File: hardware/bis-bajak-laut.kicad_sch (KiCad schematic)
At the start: 1 part, among them U1 RP2040

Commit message: feat: copying schematic part 1
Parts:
- added C1, C2, C3, C4, C6, C8: 100nF, Capacitor_SMD:C_0805_2012Metric_Pad1.18x1.45mm_HandSolder, symbol Device:C
- added C5, C7, C9: 2.2uF, Capacitor_SMD:C_0805_2012Metric_Pad1.18x1.45mm_HandSolder, symbol Device:C
- added D2, D3, D4, D5, D6: BAS40-05T, symbol Device:D_Schottky_Dual_CommonCathode_AAK
- added J1: TFT, symbol Connector_Generic:Conn_01x09
- added Q1, Q2, Q3, Q4, Q5, Q6, Q7, Q8: Q_PMOS_GSD, symbol Device:Q_PMOS_GSD
- added Q9: Q_NMOS_GSD, symbol Device:Q_NMOS_GSD
- added R1: 10K, Resistor_SMD:R_0805_2012Metric_Pad1.20x1.40mm_HandSolder, symbol Device:R_US
- added R10, R11, R12, R13, R14, R2, R25, R26, R27, R28, R29, R3, R30, R31, R32, R33, R34, R35, R36, R4, R5, R6, R7, R8, R9: 510, Resistor_SMD:R_0805_2012Metric_Pad1.20x1.40mm_HandSolder, symbol Device:R_US
- added R15, R16, R17, R18, R19, R20, R21, R22, R23, R24, R37, R38: 10k, Resistor_SMD:R_0805_2012Metric_Pad1.20x1.40mm_HandSolder, symbol Device:R_US
- added R39: 100K, Resistor_SMD:R_0805_2012Metric_Pad1.20x1.40mm_HandSolder, symbol Device:R_US
- added R40: 200, Resistor_SMD:R_0805_2012Metric_Pad1.20x1.40mm_HandSolder, symbol Device:R_US
- added R41: 33, Resistor_SMD:R_0805_2012Metric_Pad1.20x1.40mm_HandSolder, symbol Device:R_US
- added U2, U6: 74HC595, Package_SO:SOIC-16_3.9x9.9mm_P1.27mm, symbol 74xx:74HC595
- added U3, U7, U8: LMV324, Package_SO:SOIC-14_3.9x8.7mm_P1.27mm, symbol Amplifier_Operational:LMV324
- added U4: CD74HC4067M, Package_SO:SOIC-24W_7.5x15.4mm_P1.27mm, symbol 74xx:CD74HC4067M
- added U5: 74HC245, Package_DIP:DIP-20_W8.89mm_SMDSocket_LongPads, symbol 74xx:74HC245
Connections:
- new net: R26.1, U4.8 (I1)
- new net: Q1.3 (D), R16.1
- new net: Q4.3 (D), R17.1
- new net: R3.1, U5.17 (B1)
- new net: U2.1 (QB), U5.6 (A4)
- new net: U2.15 (QA), U5.2 (A0)
- new net: U2.2 (QC), U5.5 (A3)
- new net: U2.3 (QD), U5.4 (A2)
- new net: U2.4 (QE), U5.3 (A1)
- new net: U2.7 (QH), U5.9 (A7)
- new net: U2.9 (QH'), U6.14 (SER)
- new net: Q3.3 (D), R15.1
- new net: D4.2 (A), R12.2, U7.5 (+)
- new net: D4.1 (A), R11.2, U7.3 (+)
- new net: D5.2 (A), R14.2, U7.12 (+)
- new net: R28.1, U4.6 (I3)
- new net: D3.1 (A), R8.2, U3.10 (+)
- new net: R2.1, U5.18 (B0)
- new net: U4.1 (COM), U8.3 (+)
- new net: R32.1, U4.2 (I7)
- new net: R36.1, U4.20 (I11)
- new net: R35.1, U4.21 (I10)
- new net: R34.1, U4.22 (I9)
- new net: R33.1, U4.23 (I8)
- new net: R31.1, U4.3 (I6)
- new net: R30.1, U4.4 (I5)
- new net: R29.1, U4.5 (I4)
- new net: R27.1, U4.7 (I2)
- new net: R25.1, U4.9 (I0)
- new net: D3.2 (A), R9.2, U3.12 (+)
- new net: D5.1 (A), R13.2, U7.10 (+)
- new net: D2.1 (A), R7.2, U3.3 (+)
- new net: D2.2 (A), R10.2, U3.5 (+)
- new net: R5.1, U5.15 (B3)
- new net: Q7.3 (D), R23.1
- new net: Q8.3 (D), R21.1
- new net: Q9.1 (G), R40.1
- new net: Q5.3 (D), R20.1
- new net: Q9.3 (D), R41.2
- new net: R6.1, U5.14 (B4)
- new net: Q6.3 (D), R22.1
- new net: D6.1 (A), R39.1, U8.5 (+)
- new net: R4.1, U5.16 (B2)
- new net: Q2.3 (D), R18.1
- new net: R37.2, U8.1, U8.2 (-)
- new net +3V3: C1.1, C2.1, C3.1, J1.4 (Pin_4), R1.1, U2.10 (~{SRCLR}), U2.16 (VCC), U5.20 (VCC), U6.10 (~{SRCLR}), U6.16 (VCC)
- new net AMUX_EN: R2.2, R24.2, U4.15 (~{E})
- new net AMUX_OUT: R37.1, R38.1
- new net AMUX_S0: R6.2, U4.10 (S0)
- new net AMUX_S1: R5.2, U4.11 (S1)
- new net AMUX_S2: R4.2, U4.14 (S2)
- new net AMUX_S3: R3.2, U4.13 (S3)
- new net BPIO0: R14.1, R23.2
- new net BPIO1: R13.1, R22.2
- new net BPIO2: R12.1, R21.2
- new net BPIO3: R11.1, R20.2
- new net BPIO4: R18.2, R9.1
- new net BPIO5: R17.2, R8.1
- new net BPIO6: R10.1, R16.2
- new net BPIO7: R15.2, R7.1
- new net CURRENT_EN: U6.1 (QB)
- new net CURRENT_EN_OVERRIDE: U6.5 (QF)
- new net CURRENT_RESET: U6.3 (QD)
- new net DAC_RESET: U6.4 (QE)
- new net DISPLAY_BACKLIGHT: R40.2, U2.5 (QF)
- new net DISPLAY_CS: J1.6 (Pin_6)
- new net DISPLAY_DP: J1.5 (Pin_5)
- new net DISPLAY_LED_K: J1.2 (Pin_2), R41.1
- new net DISPLAY_RESET: J1.9 (Pin_9), U2.6 (QG)
- new net GND: C1.2, C2.2, C3.2, C4.2, C5.2, C6.2, C7.2, C8.2, C9.2, J1.1 (Pin_1), Q9.2 (S), R38.2, U2.8 (GND), U3.11 (V-), U4.12 (GND), U4.16 (I15), U4.17 (I14), U4.18 (I13), U4.19 (I12), U5.10 (GND), U5.8 (A6), U6.8 (GND), U7.11 (V-), U8.11 (V-)
- new net LEDS_CD0: U5.13 (B5)
- new net MUX_BPIO0: U7.13 (-), U7.14
- new net MUX_BPIO1: U7.8, U7.9 (-)
- new net MUX_BPIO2: U7.6 (-), U7.7
- new net MUX_BPIO3: U7.1, U7.2 (-)
- new net MUX_BPIO4: U3.13 (-), U3.14
- new net MUX_BPIO5: U3.8, U3.9 (-)
- new net MUX_BPIO6: U3.6 (-), U3.7
- new net MUX_BPIO7: U3.1, U3.2 (-)
- new net MUX_VREF_OUT: U8.6 (-), U8.7
- new net PULLUP_EN: Q1.1 (G), Q2.1 (G), Q3.1 (G), Q4.1 (G), Q5.1 (G), Q6.1 (G), Q7.1 (G), Q8.1 (G), R19.1, U5.11 (B7)
- new net RGB_CD0: U5.7 (A5)
- new net SHIFT_EN: R1.2, U2.13 (~{OE}), U5.19 (CE), U6.13 (~{OE})
- new net SHIFT_LATCH: U2.12 (RCLK), U6.12 (RCLK)
- new net SPI_CD0: J1.8 (Pin_8), U2.14 (SER)
- new net SPI_CLK: J1.7 (Pin_7), U2.11 (SRCLK), U6.11 (SRCLK)
- new net VBUS: C4.1, C5.1, C6.1, C7.1, C8.1, C9.1, D2.3 (K), D3.3 (K), D4.3 (K), D5.3 (K), D6.3 (K), J1.3 (Pin_3), R19.2, R24.1, U3.4 (V+), U4.24 (VCC), U5.1 (A->B), U7.4 (V+), U8.4 (V+)
- new net VREF_OUT: Q1.2 (S), Q2.2 (S), Q3.2 (S), Q4.2 (S), Q5.2 (S), Q6.2 (S), Q7.2 (S), Q8.2 (S), R39.2
- no-connect marks 0 -> 7
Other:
- company: (none) -> Crumbs Module
- title: (none) -> Bis Bajak Laut - Bus Pirate Copy From Scratch
- moved on the sheet: U1

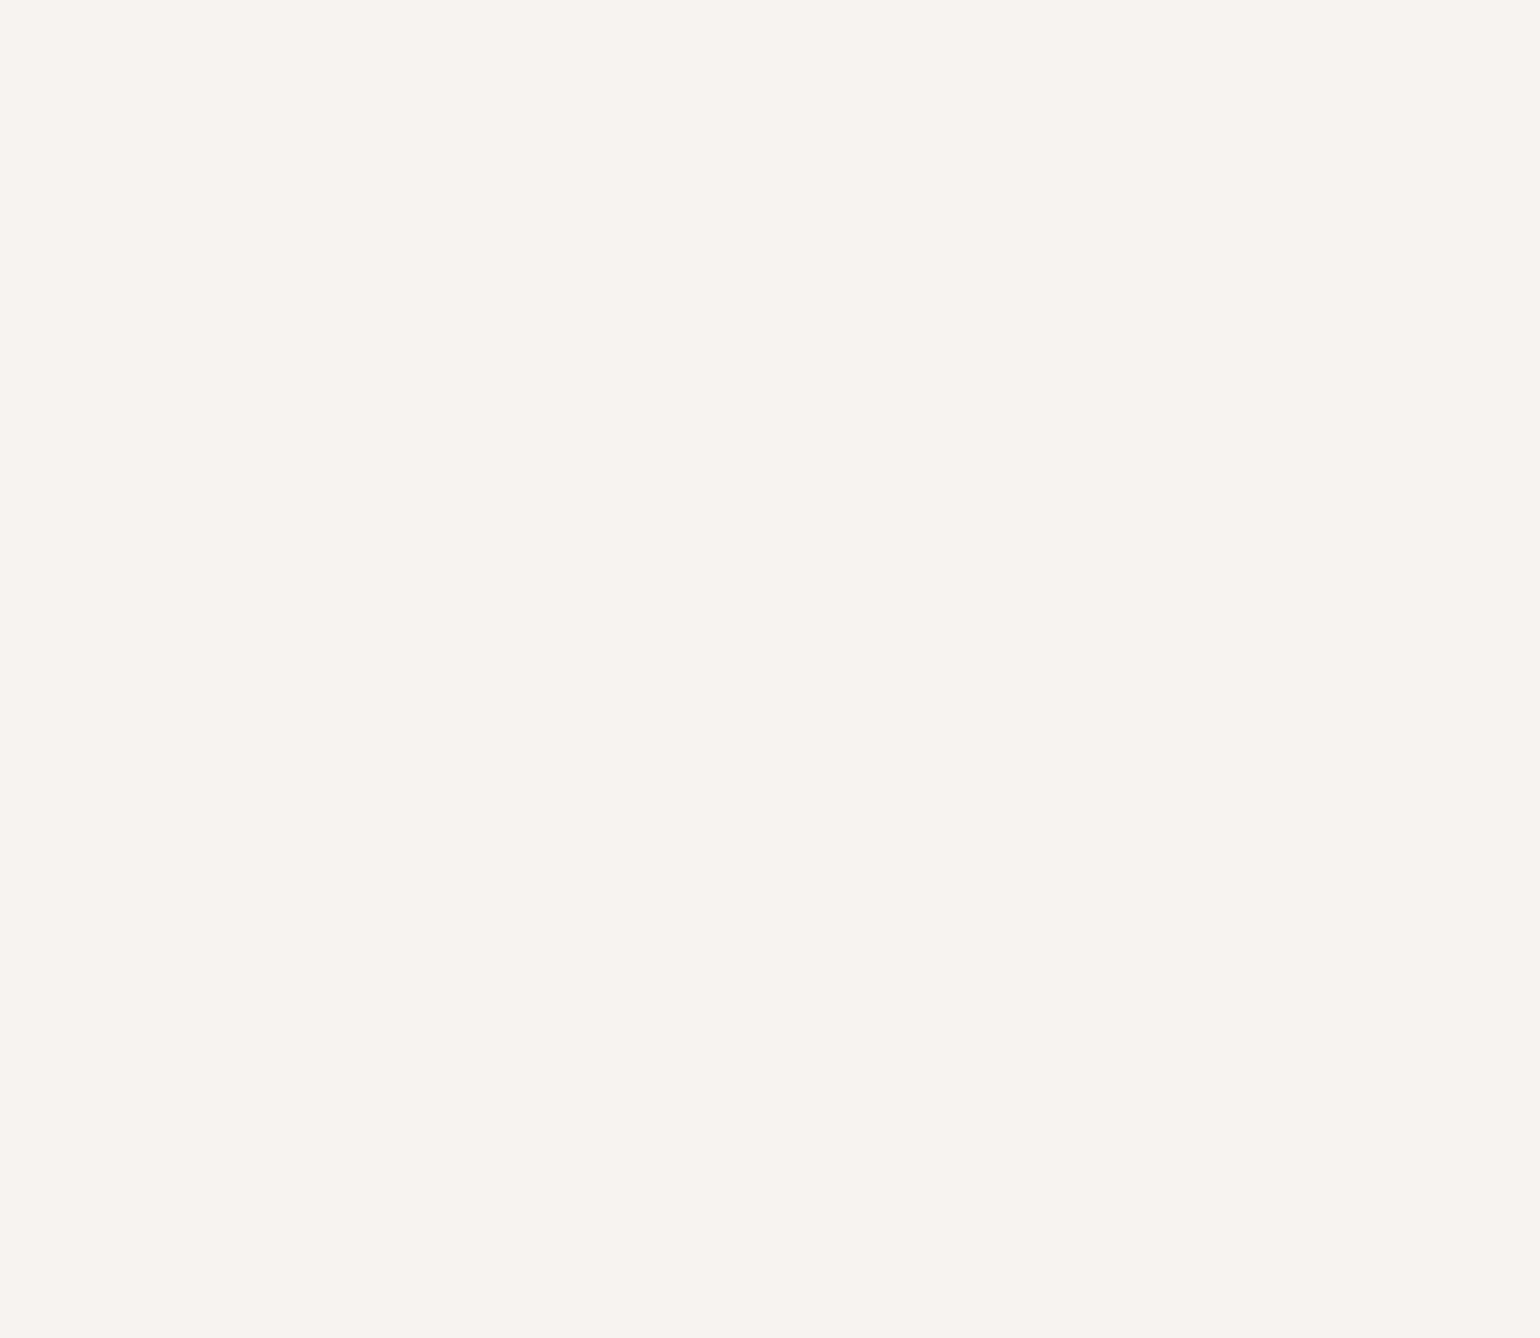
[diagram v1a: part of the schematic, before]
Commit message: feat: copying schematic part 2
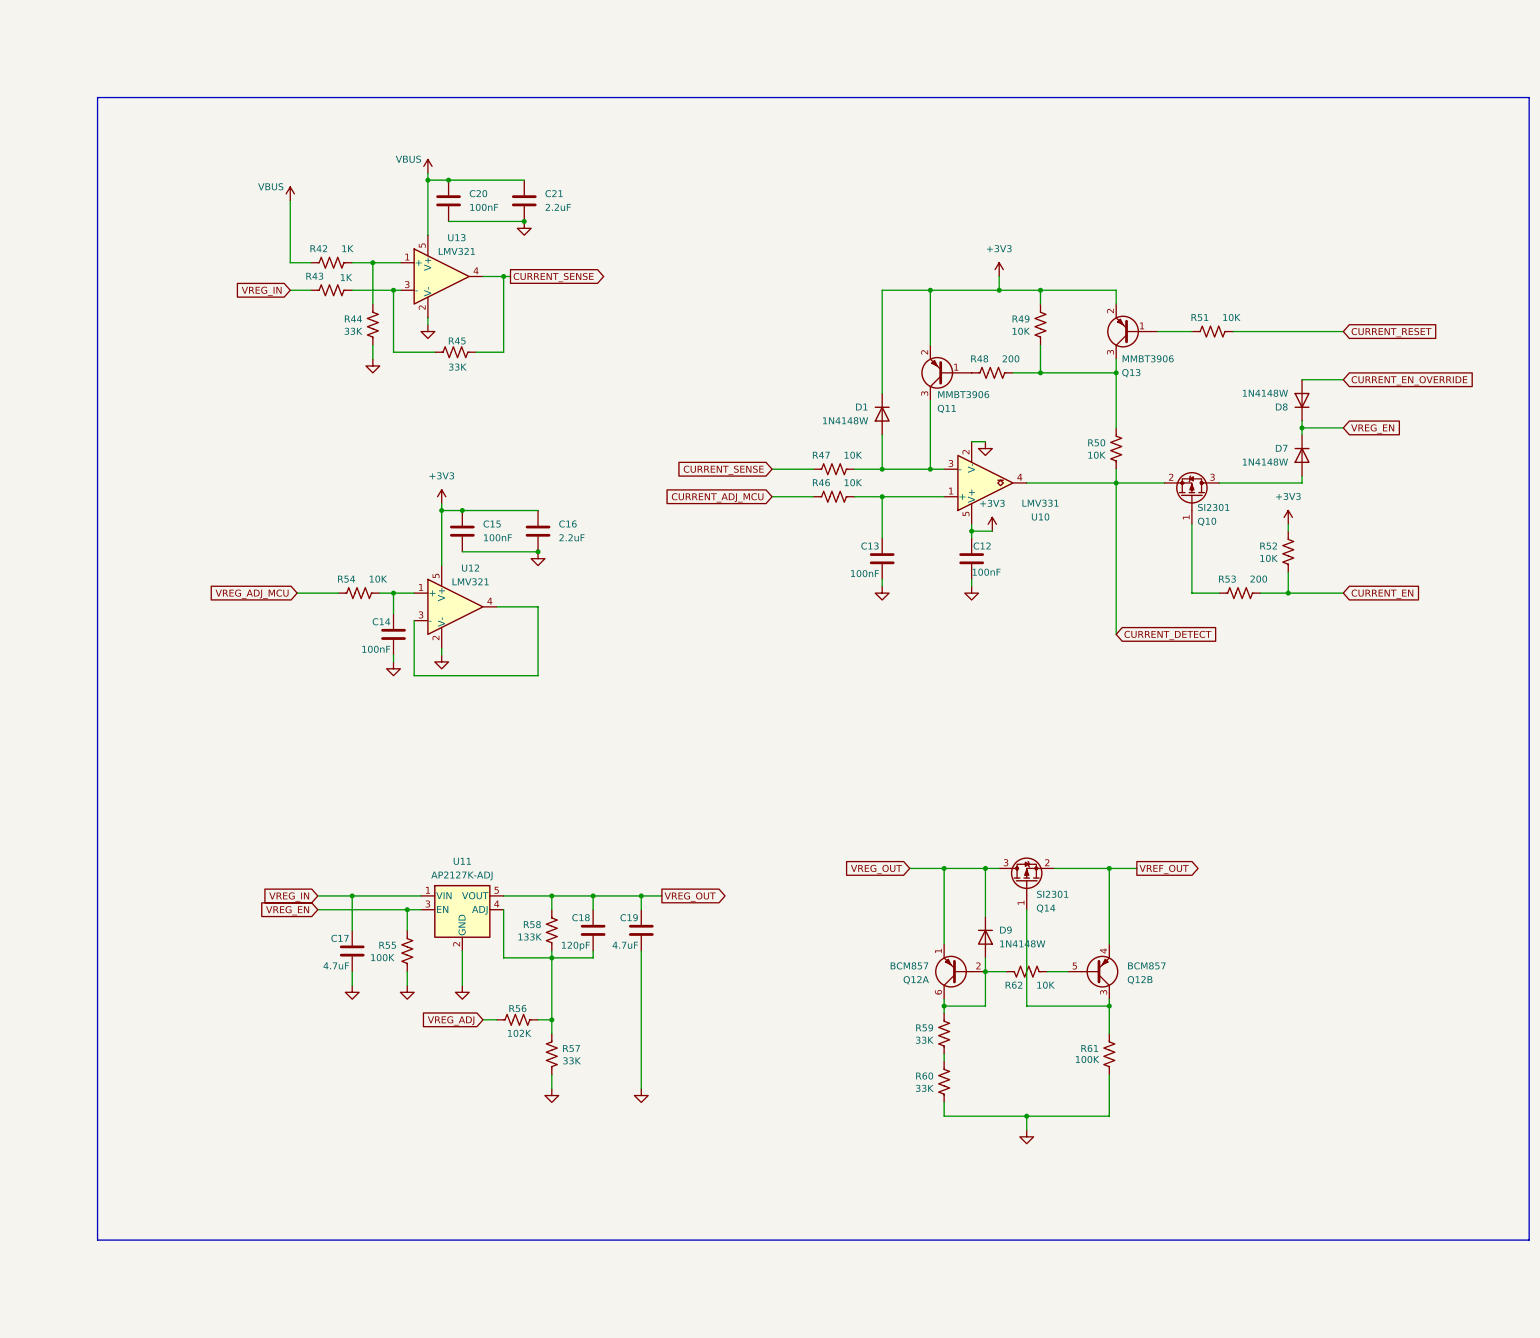
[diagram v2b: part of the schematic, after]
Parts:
- added C12, C13, C14, C15, C20: 100nF, Capacitor_SMD:C_0805_2012Metric_Pad1.18x1.45mm_HandSolder, symbol Device:C
- added C16, C21: 2.2uF, Capacitor_SMD:C_0805_2012Metric_Pad1.18x1.45mm_HandSolder, symbol Device:C
- added C17, C19: 4.7uF, Capacitor_SMD:C_0805_2012Metric_Pad1.18x1.45mm_HandSolder, symbol Device:C
- added C18: 120pF, Capacitor_SMD:C_0805_2012Metric_Pad1.18x1.45mm_HandSolder, symbol Device:C
- added D1, D7, D8, D9: 1N4148W, Diode_SMD:D_SOD-123, symbol Diode:1N4148W
- added Q10, Q14: SI2301, symbol Device:Q_PMOS_GSD
- added Q11, Q13: MMBT3906, Package_TO_SOT_SMD:SOT-23, symbol Transistor_BJT:MMBT3906
- added Q12: BCM857, Package_TO_SOT_SMD:SOT-363_SC-70-6_Handsoldering, symbol Device:Q_Dual_PNP_PNP_E1B1C2E2B2C1
- added R42, R43: 1K, Resistor_SMD:R_0805_2012Metric_Pad1.20x1.40mm_HandSolder, symbol Device:R_US
- added R44, R45, R57, R59, R60: 33K, Resistor_SMD:R_0805_2012Metric_Pad1.20x1.40mm_HandSolder, symbol Device:R_US
- added R46, R47, R49, R50, R51, R52, R54, R62: 10K, Resistor_SMD:R_0805_2012Metric_Pad1.20x1.40mm_HandSolder, symbol Device:R_US
- added R48, R53: 200, Resistor_SMD:R_0805_2012Metric_Pad1.20x1.40mm_HandSolder, symbol Device:R_US
- added R55, R61: 100K, Resistor_SMD:R_0805_2012Metric_Pad1.20x1.40mm_HandSolder, symbol Device:R_US
- added R56: 102K, Resistor_SMD:R_0805_2012Metric_Pad1.20x1.40mm_HandSolder, symbol Device:R_US
- added R58: 133K, Resistor_SMD:R_0805_2012Metric_Pad1.20x1.40mm_HandSolder, symbol Device:R_US
- added U10: LMV331, Package_TO_SOT_SMD:SOT-23-5_HandSoldering, symbol Comparator:LMV331
- added U11: AP2127K-ADJ, Package_TO_SOT_SMD:SOT-23-5, symbol Regulator_Linear:AP2127K-ADJ
- added U12, U13: LMV321, symbol Amplifier_Operational:LMV321
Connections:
- net +3V3: now also C12.1, C15.1, C16.1, D1.1 (K), Q11.2 (E), Q13.2 (E), R49.1, R52.1, U10.5 (V+), U12.5 (V+)
- net CURRENT_EN: now also R52.2, R53.1
- net CURRENT_EN_OVERRIDE: now also D8.2 (A)
- net CURRENT_RESET: now also R51.1
- net GND: now also C12.2, C13.2, C14.2, C15.2, C16.2, C17.2, C19.2, C20.2, C21.2, R44.2, R55.2, R57.2, R60.2, R61.2, U10.2 (V-), U11.2 (GND), U12.2 (V-), U13.2 (V-)
- net VBUS: now also C20.1, C21.1, R42.2, U13.5 (V+)
- net VREF_OUT: now also Q12.4 (E2), Q14.2 (S)
- new net: R43.1, R45.1, U13.3 (-)
- new net: Q13.1 (B), R51.2
- new net: D9.2 (A), Q12.2 (B1), Q12.6 (C1), R59.1, R62.2
- new net: R59.2, R60.1
- new net: Q11.1 (B), R48.2
- new net: D1.2 (A), Q11.3 (C), R47.1, U10.3 (-)
- new net: C18.2, R56.2, R57.1, R58.2, U11.4 (ADJ)
- new net: Q12.3 (C2), Q14.1 (G), R61.1
- new net: C13.1, R46.1, U10.1 (+)
- new net: Q13.3 (C), R48.1, R49.2, R50.1
- new net: C14.1, R54.1, U12.1 (+)
- new net: R42.1, R44.1, U13.1 (+)
- new net: U12.3 (-), U12.4
- new net: Q12.5 (B2), R62.1
- new net: Q10.1 (G), R53.2
- new net: D7.2 (A), Q10.3 (D)
- new net CURRENT_ADJ_MCU: R46.2
- new net CURRENT_DETECT: Q10.2 (S), R50.2, U10.4
- new net CURRENT_SENSE: R45.2, R47.2, U13.4
- new net VREG_ADJ: R56.1
- new net VREG_ADJ_MCU: R54.2
- new net VREG_EN: D7.1 (K), D8.1 (K), R55.1, U11.3 (EN)
- new net VREG_IN: C17.1, R43.2, U11.1 (VIN)
- new net VREG_OUT: C18.1, C19.1, D9.1 (K), Q12.1 (E1), Q14.3 (D), R58.1, U11.5 (VOUT)

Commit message: feat: finish copying schematic
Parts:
- removed Q8: Q_PMOS_GSD, symbol Device:Q_PMOS_GSD
- removed Q9: Q_NMOS_GSD, symbol Device:Q_NMOS_GSD
- removed U1: RP2040, Package_DFN_QFN:QFN-56-1EP_7x7mm_P0.4mm_EP3.2x3.2mm, symbol MCU_RaspberryPi:RP2040
- added C10, C11: 4.7uF, Capacitor_SMD:C_0805_2012Metric_Pad1.18x1.45mm_HandSolder, symbol Device:C
- added C22, C23, C24, C25, C26, C27, C28, C29, C30, C33, C39, C40, C41, C42, C43, C44, C45, C46, C47, C48, C49, C50, C51, C52, C53, C54, C55, C56, C57, C58, C59, C60, C61, C62, C63, C64, C65, C66, C67, C68, C69, C70, C71, C72: 100nF, Capacitor_SMD:C_0805_2012Metric_Pad1.18x1.45mm_HandSolder, symbol Device:C
- added C31, C32, C34: 2.2uF, Capacitor_SMD:C_0805_2012Metric_Pad1.18x1.45mm_HandSolder, symbol Device:C
- added C35, C36: 15pF, Capacitor_SMD:C_0805_2012Metric_Pad1.18x1.45mm_HandSolder, symbol Device:C
- added C37, C38: 22uF, Capacitor_SMD:C_0805_2012Metric_Pad1.18x1.45mm_HandSolder, symbol Device:C
- added D10: PWR, LED_SMD:LED_1206_3216Metric_Pad1.42x1.75mm_HandSolder, symbol Device:LED
- added D11, D12, D13, D14, D15, D16, D17, D18, D19, D20, D21, D22, D23, D24, D25, D26, D27, D28: WS2812B-2020, LED_SMD:LED_WS2812B-2020_PLCC4_2.0x2.0mm, symbol LED:WS2812B-2020
- added J2: USB_C_Receptacle_USB2.0_14P, symbol Connector:USB_C_Receptacle_USB2.0_14P
- added J3: ProgHeader, symbol Connector_Generic:Conn_01x03
- added J4, J5: BIS BAJAK LAUT IO, Connector_PinHeader_2.54mm:PinHeader_1x10_P2.54mm_Vertical, symbol Connector_Generic:Conn_01x10
- added Q8: Q_NMOS_GSD, symbol Device:Q_NMOS_GSD
- added Q9: Q_PMOS_GSD, symbol Device:Q_PMOS_GSD
- added R100, R103, R106, R68, R69, R70, R71, R72, R73, R74, R75, R77, R80, R83, R86, R88, R89, R90, R91, R92, R93, R94, R95, R97: 330, Resistor_SMD:R_0805_2012Metric_Pad1.20x1.40mm_HandSolder, symbol Device:R_US
- added R101, R104, R107, R78, R81, R84, R87, R98: 1M, Resistor_SMD:R_0805_2012Metric_Pad1.20x1.40mm_HandSolder, symbol Device:R_US
- added R102, R105, R76, R79, R82, R85, R96, R99: 100K, Resistor_SMD:R_0805_2012Metric_Pad1.20x1.40mm_HandSolder, symbol Device:R_US
- added R108: 10K, Resistor_SMD:R_0805_2012Metric_Pad1.20x1.40mm_HandSolder, symbol Device:R_US
- added R63, R64: 5K1, Resistor_SMD:R_0805_2012Metric_Pad1.20x1.40mm_HandSolder, symbol Device:R_US
- added R65: 200, Resistor_SMD:R_0805_2012Metric_Pad1.20x1.40mm_HandSolder, symbol Device:R_US
- added R66, R67: 1K, Resistor_SMD:R_0805_2012Metric_Pad1.20x1.40mm_HandSolder, symbol Device:R_US
- added SW1: W25Sel, symbol Switch:SW_Push
- added SW2: BUTTON, symbol Switch:SW_Push
- added U1: MT29F1G01ABAFDWB, dp-memory:U-PDFN-8, symbol dp-memory:MT29F1G01ABAFDWB
- added U14: W25Q128JVS, Package_SO:SOIC-8_5.23x5.23mm_P1.27mm, symbol Memory_Flash:W25Q128JVS
- added U15: AMS1117-3.3, Package_TO_SOT_SMD:SOT-223-3_TabPin2, symbol Regulator_Linear:AMS1117-3.3
- added U16, U17, U18, U19, U20, U21, U22, U23: SN74LVC1T45DRL, Package_TO_SOT_SMD:SOT-563, symbol Logic_LevelTranslator:SN74LVC1T45DRL
- added U9: RP2040, Package_DFN_QFN:QFN-56-1EP_7x7mm_P0.4mm_EP3.2x3.2mm, symbol MCU_RaspberryPi:RP2040
- added Y1: 12Mhz, symbol Device:Crystal_GND24_Small
- R20: value 10k -> 33
- R23: value 10k -> 200
- R40: value 200 -> 10k
- R41: value 33 -> 10k
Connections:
- net +3V3: now also C22.1, C23.1, C24.1, C25.1, C26.1, C27.1, C28.1, C33.1, C34.1, C38.1, C39.1, C41.1, C43.1, C45.1, C47.1, C49.1, C51.1, C53.1, D10.2 (A), R65.1, SW2.1, U1.3 (WP/IO2), U1.7 (HOLD/IO3), U1.8 (VCC), U14.8 (VCC), U15.2 (VO), U16.1 (VCCA), U17.1 (VCCA), U18.1 (VCCA), U19.1 (VCCA), U20.1 (VCCA), U21.1 (VCCA), U22.1 (VCCA), U23.1 (VCCA), U9.1 (IOVDD), U9.10 (IOVDD), U9.22 (IOVDD), U9.26 (RUN), U9.33 (IOVDD), U9.42 (IOVDD), U9.44 (VREG_IN), U9.48 (USB_VDD), U9.49 (IOVDD)
- net AMUX_OUT: now also U9.40 (GPIO28_ADC2)
- net BPIO0: now also R21.2, J4.2 (Pin_2), J5.2 (Pin_2), R69.2; no longer R23.2
- net BPIO1: now also J4.3 (Pin_3), J5.3 (Pin_3), R71.2
- net BPIO2: now also R40.2, J4.4 (Pin_4), J5.4 (Pin_4), R73.2; no longer R21.2
- net BPIO3: now also R41.2, J4.5 (Pin_5), J5.5 (Pin_5), R75.2; no longer R20.2
- net BPIO4: now also J4.6 (Pin_6), J5.6 (Pin_6), R89.2
- net BPIO5: now also J4.7 (Pin_7), J5.7 (Pin_7), R91.2
- net BPIO6: now also J4.8 (Pin_8), J5.8 (Pin_8), R93.2
- net BPIO7: now also J4.9 (Pin_9), J5.9 (Pin_9), R95.2
- net CURRENT_ADJ_MCU: now also U9.34 (GPIO22)
- net CURRENT_DETECT: now also R34.2
- net CURRENT_SENSE: now also U9.41 (GPIO29_ADC3)
- net DISPLAY_BACKLIGHT: now also R23.2; no longer R40.2
- net DISPLAY_CS: now also U9.37 (GPIO25)
- net DISPLAY_DP: now also U9.36 (GPIO24)
- net DISPLAY_LED_K: now also R20.1; no longer R41.1
- net GND: now also C10.2, C11.2, C22.2, C23.2, C24.2, C25.2, C26.2, C27.2, C28.2, C29.2, C30.2, C31.2, C32.2, C33.2, C34.2, C35.1, C36.1, C37.2, C38.2, C39.2, C40.2, C41.2, C42.2, C43.2, C44.2, C45.2, C46.2, C47.2, C48.2, C49.2, C50.2, C51.2, C52.2, C53.2, C54.2, C55.2, C56.2, C57.2, C58.2, C59.2, C60.2, C61.2, C62.2, C63.2, C64.2, C65.2, C66.2, C67.2, C68.2, C69.2, C70.2, C71.2, C72.2, D11.2 (VSS), D12.2 (VSS), D13.2 (VSS), D14.2 (VSS), D15.2 (VSS), D16.2 (VSS), D17.2 (VSS), D18.2 (VSS), D19.2 (VSS), D20.2 (VSS), D21.2 (VSS), D22.2 (VSS), D23.2 (VSS), D24.2 (VSS), D25.2 (VSS), D26.2 (VSS), D27.2 (VSS), D28.2 (VSS), J2.A1 (GND), J2.A12 (GND), J2.B1 (GND), J2.B12 (GND), J3.1 (Pin_1), J4.10 (Pin_10), J5.10 (Pin_10), Q8.2 (S), R100.2, R101.2, R102.2, R103.2, R104.2, R105.2, R106.2, R107.2, R108.2, R63.2, R64.2, R67.2, R76.2, R77.2, R78.2, R79.2, R80.2, R81.2, R82.2, R83.2, R84.2, R85.2, R86.2, R87.2, R96.2, R97.2, R98.2, R99.2, SW1.1, U1.4 (VSS), U14.4 (GND), U15.1 (GND), U16.2 (GND), U17.2 (GND), U18.2 (GND), U19.2 (GND), U20.2 (GND), U21.2 (GND), U22.2 (GND), U23.2 (GND), U9.19 (TESTEN), U9.57 (GND), Y1.2, Y1.4
- net LEDS_CD0: now also D11.3 (DIN)
- net MUX_BPIO0: now also R32.2
- net MUX_BPIO1: now also R31.2
- net MUX_BPIO2: now also R30.2
- net MUX_BPIO3: now also R29.2
- net MUX_BPIO4: now also R28.2
- net MUX_BPIO5: now also R27.2
- net MUX_BPIO6: now also R26.2
- net MUX_BPIO7: now also R25.2
- net MUX_VREF_OUT: now also R36.2
- net PULLUP_EN: now also Q9.1 (G)
- net RGB_CD0: now also U9.28 (GPIO17)
- net SHIFT_EN: now also U9.32 (GPIO21)
- net SHIFT_LATCH: now also U9.31 (GPIO20)
- net SPI_CD0: now also U1.5 (SI/IO0), U9.30 (GPIO19)
- net SPI_CLK: now also U1.6 (SCK), U9.29 (GPIO18)
- net VBUS: now also R33.2, C10.1, C11.1, C37.1, C55.1, C56.1, C57.1, C58.1, C59.1, C60.1, C61.1, C62.1, C63.1, C64.1, C65.1, C66.1, C67.1, C68.1, C69.1, C70.1, C71.1, C72.1, D11.4 (VDD), D12.4 (VDD), D13.4 (VDD), D14.4 (VDD), D15.4 (VDD), D16.4 (VDD), D17.4 (VDD), D18.4 (VDD), D19.4 (VDD), D20.4 (VDD), D21.4 (VDD), D22.4 (VDD), D23.4 (VDD), D24.4 (VDD), D25.4 (VDD), D26.4 (VDD), D27.4 (VDD), D28.4 (VDD), J2.A4 (VBUS), J2.A9 (VBUS), J2.B4 (VBUS), J2.B9 (VBUS), U15.3 (VI)
- net VREF_OUT: now also C40.1, C42.1, C44.1, C46.1, C48.1, C50.1, C52.1, C54.1, J4.1 (Pin_1), J5.1 (Pin_1), Q9.2 (S), R108.1, U16.6 (VCCB), U17.6 (VCCB), U18.6 (VCCB), U19.6 (VCCB), U20.6 (VCCB), U21.6 (VCCB), U22.6 (VCCB), U23.6 (VCCB)
- net VREG_ADJ_MCU: now also U9.35 (GPIO23)
- net VREG_OUT: now also R35.2
- net at R16.1: now also Q4.3 (D); no longer Q1.3 (D)
- net at R17.1: now also Q2.3 (D); no longer Q4.3 (D)
- net at Q3.3 (D): now also R18.1; no longer R15.1
- net at Q7.3 (D): now also R22.1; no longer R23.1
- net at R21.1: now also Q6.3 (D)
- net at R40.1: now also Q5.3 (D)
- new net: J2.B5 (CC2), R64.1
- new net: D27.1 (DOUT), D28.3 (DIN)
- new net: R75.1, R87.1, U19.4 (B)
- new net: R100.1, R90.2, U21.3 (A)
- new net: R70.2, R80.1, U17.3 (A)
- new net: R88.2, R97.1, U20.3 (A)
- new net: R89.1, R98.1, U20.4 (B)
- new net: D17.1 (DOUT), D18.3 (DIN)
- new net: D16.1 (DOUT), D17.3 (DIN)
- new net: D10.1 (K), R67.1
- new net: R107.1, R95.1, U23.4 (B)
- new net: R72.2, R83.1, U18.3 (A)
- new net: R73.1, R84.1, U18.4 (B)
- new net: D15.1 (DOUT), D16.3 (DIN)
- new net: D14.1 (DOUT), D15.3 (DIN)
- new net: D18.1 (DOUT), D19.3 (DIN)
- new net: C32.1, R65.2, U9.43 (ADC_AVDD)
- new net: D25.1 (DOUT), D26.3 (DIN)
- new net: D24.1 (DOUT), D25.3 (DIN)
- new net: R104.1, R93.1, U22.4 (B)
- new net: C35.2, U9.20 (XIN), Y1.1
- new net: C36.2, U9.21 (XOUT), Y1.3
- new net: R101.1, R91.1, U21.4 (B)
- new net: D13.1 (DOUT), D14.3 (DIN)
- new net: R71.1, R81.1, U17.4 (B)
- new net: J2.A5 (CC1), R63.1
- new net: Q9.3 (D), R41.1
- new net: R69.1, R78.1, U16.4 (B)
- new net: R103.1, R92.2, U22.3 (A)
- new net: R66.2, SW1.2
- new net: R68.2, R77.1, U16.3 (A)
- new net: Q1.3 (D), R15.1
- new net: D20.1 (DOUT), D21.3 (DIN)
- new net: D11.1 (DOUT), D12.3 (DIN)
- new net: D21.1 (DOUT), D22.3 (DIN)
- new net: D26.1 (DOUT), D27.3 (DIN)
- new net: SW2.2, U9.39 (GPIO27_ADC1)
- new net: R106.1, R94.2, U23.3 (A)
- new net: R74.2, R86.1, U19.3 (A)
- new net: D23.1 (DOUT), D24.3 (DIN)
- new net: D22.1 (DOUT), D23.3 (DIN)
- new net: Q8.1 (G), R23.1
- new net: Q8.3 (D), R20.2
- new net: D12.1 (DOUT), D13.3 (DIN)
- new net +1V1: C29.1, C30.1, C31.1, U9.23 (DVDD), U9.45 (VREG_VOUT), U9.50 (DVDD)
- new net BUFDIR0: R76.1, U16.5 (DIR), U9.2 (GPIO0)
- new net BUFDIR1: R79.1, U17.5 (DIR), U9.3 (GPIO1)
- new net BUFDIR2: R82.1, U18.5 (DIR), U9.4 (GPIO2)
- new net BUFDIR3: R85.1, U19.5 (DIR), U9.5 (GPIO3)
- new net BUFDIR4: R96.1, U20.5 (DIR), U9.6 (GPIO4)
- new net BUFDIR5: R99.1, U21.5 (DIR), U9.7 (GPIO5)
- new net BUFDIR6: R102.1, U22.5 (DIR), U9.8 (GPIO6)
- new net BUFDIR7: R105.1, U23.5 (DIR), U9.9 (GPIO7)
- new net BUFIO0: R68.1, U9.11 (GPIO8)
- new net BUFIO1: R70.1, U9.12 (GPIO9)
- new net BUFIO2: R72.1, U9.13 (GPIO10)
- new net BUFIO3: R74.1, U9.14 (GPIO11)
- new net BUFIO4: R88.1, U9.15 (GPIO12)
- new net BUFIO5: R90.1, U9.16 (GPIO13)
- new net BUFIO6: R92.1, U9.17 (GPIO14)
- new net BUFIO7: R94.1, U9.18 (GPIO15)
- new net LED_ENDPOINT: D19.1 (DOUT), D20.3 (DIN)
- new net QSPI_CS: R66.1, U14.1 (~{CS}), U9.56 (QSPI_SS)
- new net QSPI_SCLK: U14.6 (CLK), U9.52 (QSPI_SCLK)
- new net QSPI_SD0: U14.5 (DI(IO0)), U9.53 (QSPI_SD0)
- new net QSPI_SD1: U14.2 (DO(IO1)), U9.55 (QSPI_SD1)
- new net QSPI_SD2: U14.3 (IO2), U9.54 (QSPI_SD2)
- new net QSPI_SD3: U14.7 (IO3), U9.51 (QSPI_SD3)
- new net SD_CS: U1.1 (CS), U9.38 (GPIO26_ADC0)
- new net SPI_CDI: U1.2 (SO/IO1), U9.27 (GPIO16)
- new net SWCLK: J3.3 (Pin_3), U9.24 (SWCLK)
- new net SWDIO: J3.2 (Pin_2), U9.25 (SWD)
- new net USBD+: J2.A6 (D+), J2.B6 (D+), U9.47 (USB_DP)
- new net USBD-: J2.A7 (D-), J2.B7 (D-), U9.46 (USB_DM)
- no-connect marks 7 -> 9
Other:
- note added: "BIS BAJAK LAUT"
- note added: "BUFFER IO"
- note added: "LED"
- note added: "MCU"
- note added: "POWER"
- note added: "Transceiver"
- moved on the sheet: C1, C12, C13, C14, C15, C16, C17, C18, C19, C2, C20, C21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
